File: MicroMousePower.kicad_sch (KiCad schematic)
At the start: 103 parts, among them J1 USB_C_Receptacle_PowerOnly_6P, J2 Conn_02x16_Odd_Even, J3 Conn_01x02_Pin, Q1 TIP41C, Q2 TIP41C, Q3 TIP41C, U1 INA219AxDCN, U2 MCP73831-3-MC, U3 CH224K, U4 DRV8833PWPR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

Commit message: updated pinheader footprint
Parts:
- J2: footprint Connector_PinHeader_2.54mm:PinHeader_2x16_P2.54mm_Horizontal -> Connector_PinHeader_2.54mm:PinHeader_2x16_P2.54mm_Vertical
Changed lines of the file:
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@@
 			)
 		)
-		(property "Footprint" "Connector_PinHeader_2.54mm:PinHeader_2x16_P2.54mm_Horizontal"
+		(property "Footprint" "Connector_PinHeader_2.54mm:PinHeader_2x16_P2.54mm_Vertical"
 			(at 118.11 168.91 0)
 			(effects

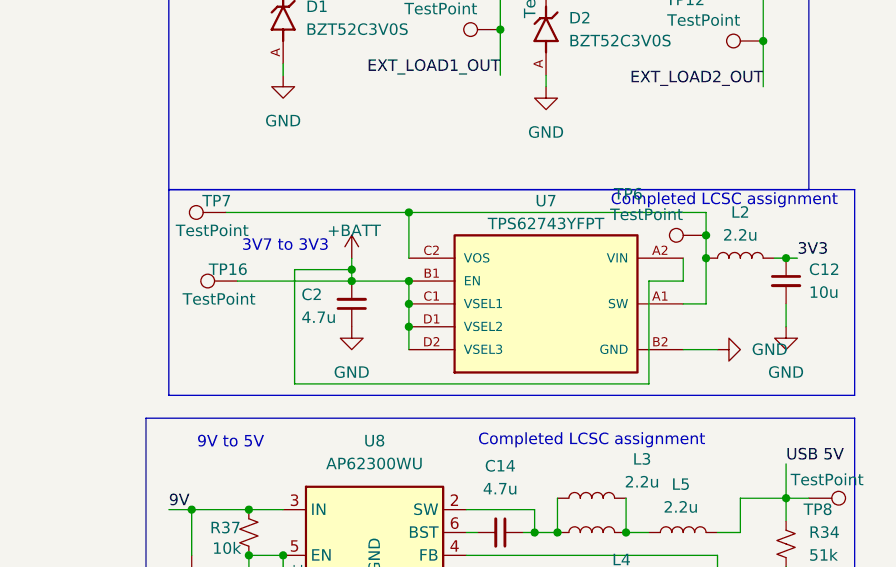
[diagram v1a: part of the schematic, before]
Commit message: updated schematic due to ordering error
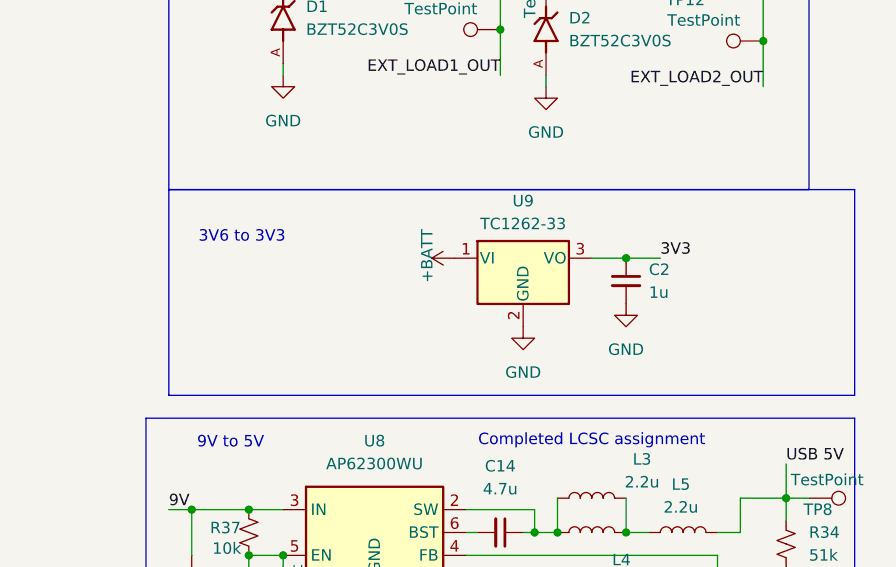
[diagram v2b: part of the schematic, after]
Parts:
- removed C12: 10u, Capacitor_SMD:C_0805_2012Metric, symbol Device:C_Small
- removed L2: 2.2u, Inductor_SMD:L_Cenker_CKCS4020, symbol Device:L
- removed TP16, TP6, TP7: TestPoint, TestPoint:TestPoint_Pad_D1.0mm, symbol Connector:TestPoint
- removed U7: TPS62743YFPT, Package_BGA:Texas_DSBGA-8_0.705x1.468mm_Layout2x4_P0.4mm, symbol TPS62743YFPT:TPS62743YFPT
- added U9: TC1262-33, Package_TO_SOT_SMD:SOT-223-3_TabPin2, symbol Regulator_Linear:TC1262-33
- C2: value 4.7u -> 1u; LCSC C1569 -> C52923
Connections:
- net +BATT: now also U9.1 (VI); no longer C2.2
- net -BATT: now also C2.2, U9.2 (GND); no longer C2.1
- net 3V3: now also C2.1, U9.3 (VO)
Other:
- note added: "3V6 to 3V3"
- note removed: "3V7 to 3V3"

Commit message: the pain never ends
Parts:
- renumbered C2 to C52
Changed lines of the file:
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@@
 		(dnp no)
 		(fields_autoplaced yes)
-		(property "Reference" "C2"
+		(property "Reference" "C52"
 			(at 261.62 118.1162 0)
 			(effects
@@
 			(project ""
 				(path "/eac97a68-d510-4c4f-b246-1e946de69ee0"
-					(reference "C2")
+					(reference "C52")
 					(unit 1)
 				)

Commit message: final submission
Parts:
- added R45, R46, R47, R48: 10, Resistor_SMD:R_1206_3216Metric, symbol Device:R_Small_US
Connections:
- net 3V3: now also R47.2, R48.2; no longer C52.1, U9.3 (VO)
- new net: C52.1, R45.1, R46.1, U9.3 (VO)
- new net: R45.2, R46.2, R47.1, R48.1

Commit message: cleaned up schematic
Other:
- note added: "Charging Modes for Battery (200mA or 600mA +-100mA)"
- note removed: "Charging Modes for Battery (200mA or 600mA ±100mA)"
- note removed: "Completed LCSC assignment"
- moved on the sheet: C13, C14, C52, L3, L4, L5, R34, R35, R36, R37, R38, R45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

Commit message: added comments
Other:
- note added: "Charges LiPo battery from the stepped down USB-C input."
- note added: "Monitors battery charging and sends data to MC via I2C."
- note added: "Negotiates 9V from the USB-C host."
- note added: "Operates 4 motors bidirectionally at 200mA and 500mA."
- note added: "Sets current used for charging battery."
- note added: "Steps down 3.7V from battery to 3.3V."
- note added: "Steps down 9V from USB-C to 5V."
- note added: "Turns voltage to loads on ando off."
- moved on the sheet: C3, J1, R10, R11, R7, R8, R9, TP17, TP18, U3
